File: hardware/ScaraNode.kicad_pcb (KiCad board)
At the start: 2 copper layers, 75.8 x 64 mm, 40 parts, among them J1 FIM1, J2 FIM2, J3 NTC, J4 DM556, J5 24V, J6 MOTOR, J7 FAN 24V, U1 RP2040-Zero, U2 74ACT245, U4 TMC2209

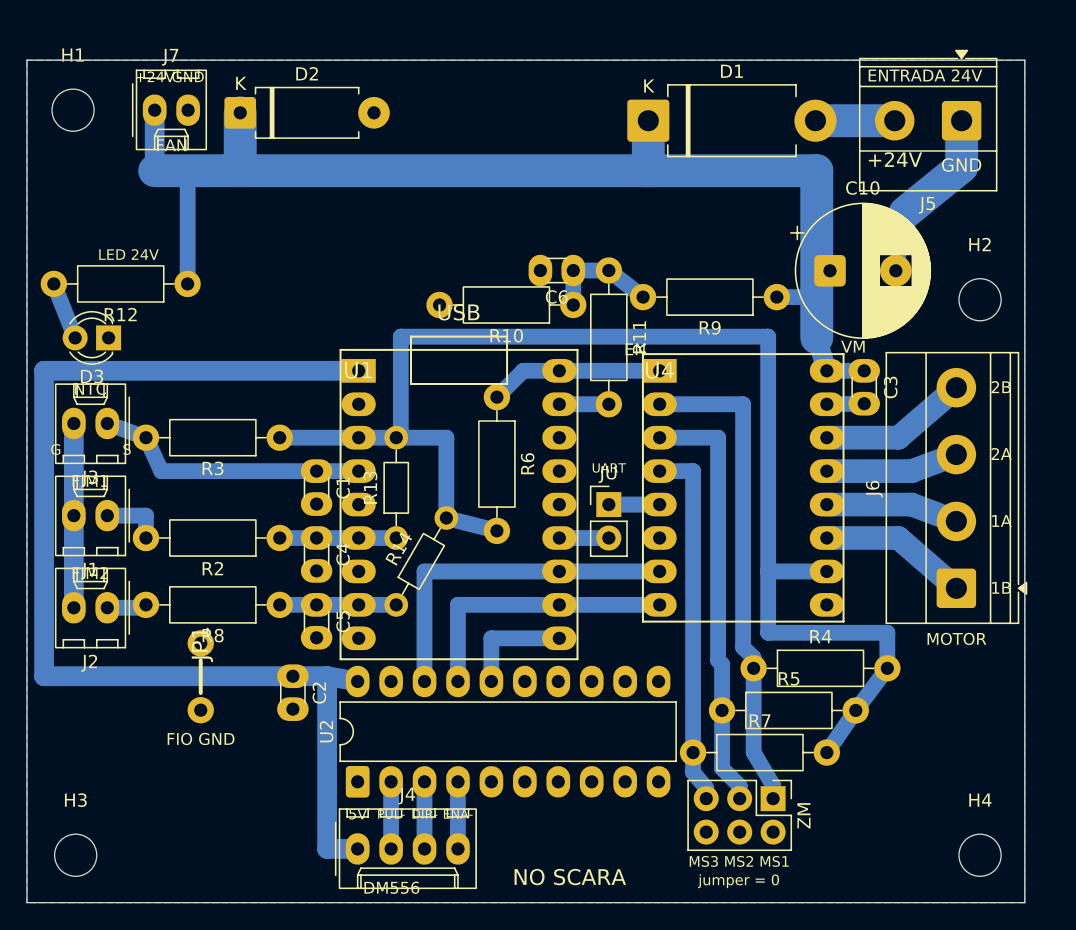
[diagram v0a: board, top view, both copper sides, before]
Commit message: docs(placa): corrige BOM e publica ScaraNode v15
Conectores JST XH (peça real), 74ACT245 soldado direto sem soquete,
borne 24 V verde e motor azul, resistores com faixas de cor por valor,
pinagem desenhada do RP2040-Zero e TMC2209 no lugar de fotos erradas.

Co-Authored-By: Claude Opus 5.5 <noreply@anthropic.com>
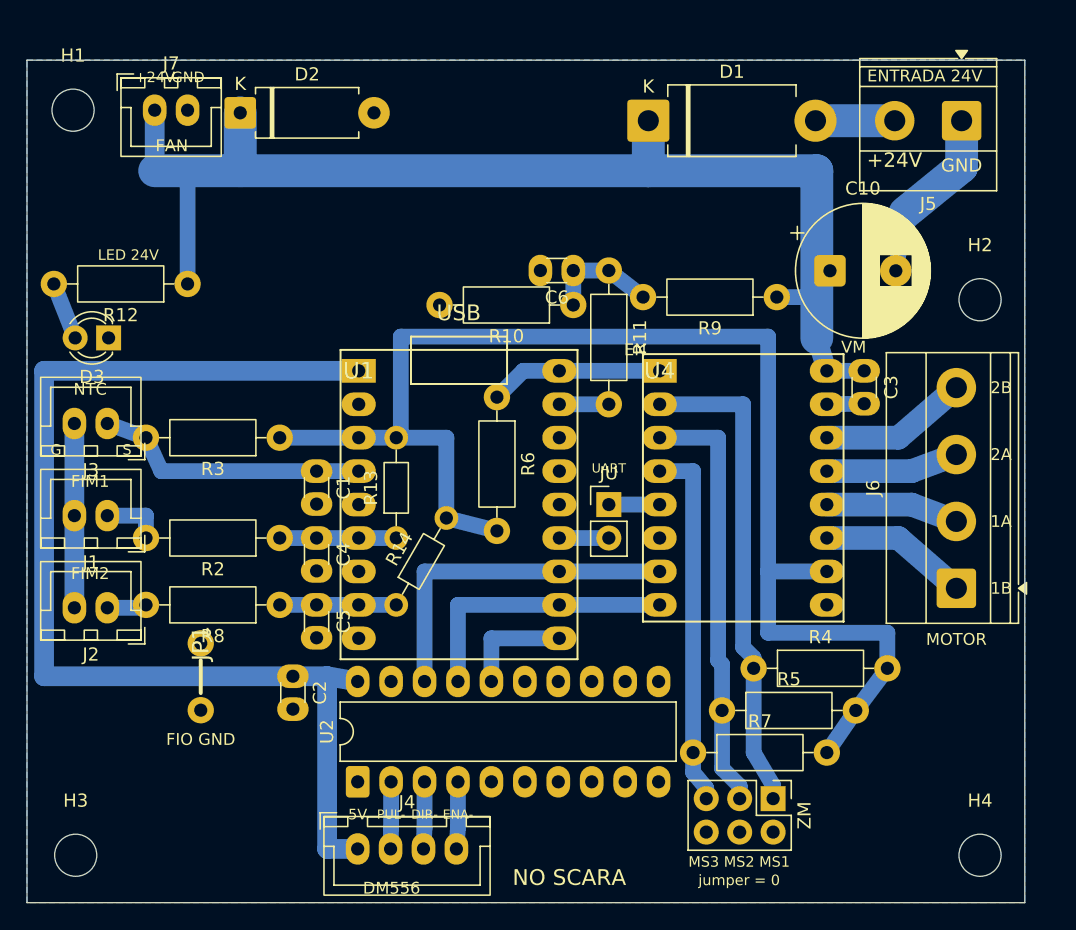
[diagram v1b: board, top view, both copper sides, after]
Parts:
- J1, J2, J3, J7: footprint Molex_KK-254_AE-6410-02A_1x02_P2.54mm_Vertical -> JST_XH_B2B-XH-A_1x02_P2.50mm_Vertical
- J4: footprint Molex_KK-254_AE-6410-04A_1x04_P2.54mm_Vertical -> JST_XH_B4B-XH-A_1x04_P2.50mm_Vertical

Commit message: docs(placa): publica ScaraNode v16
Placa 76 x 64 mm com furos M3 em retângulo de 69 x 57 mm e DXF mecânico,
74ACT245 em soquete DIP-20, borne do motor KF128 azul, NTC separado dos
fins de curso e LED de 5 mm.

Co-Authored-By: Claude Opus 5.5 <noreply@anthropic.com>
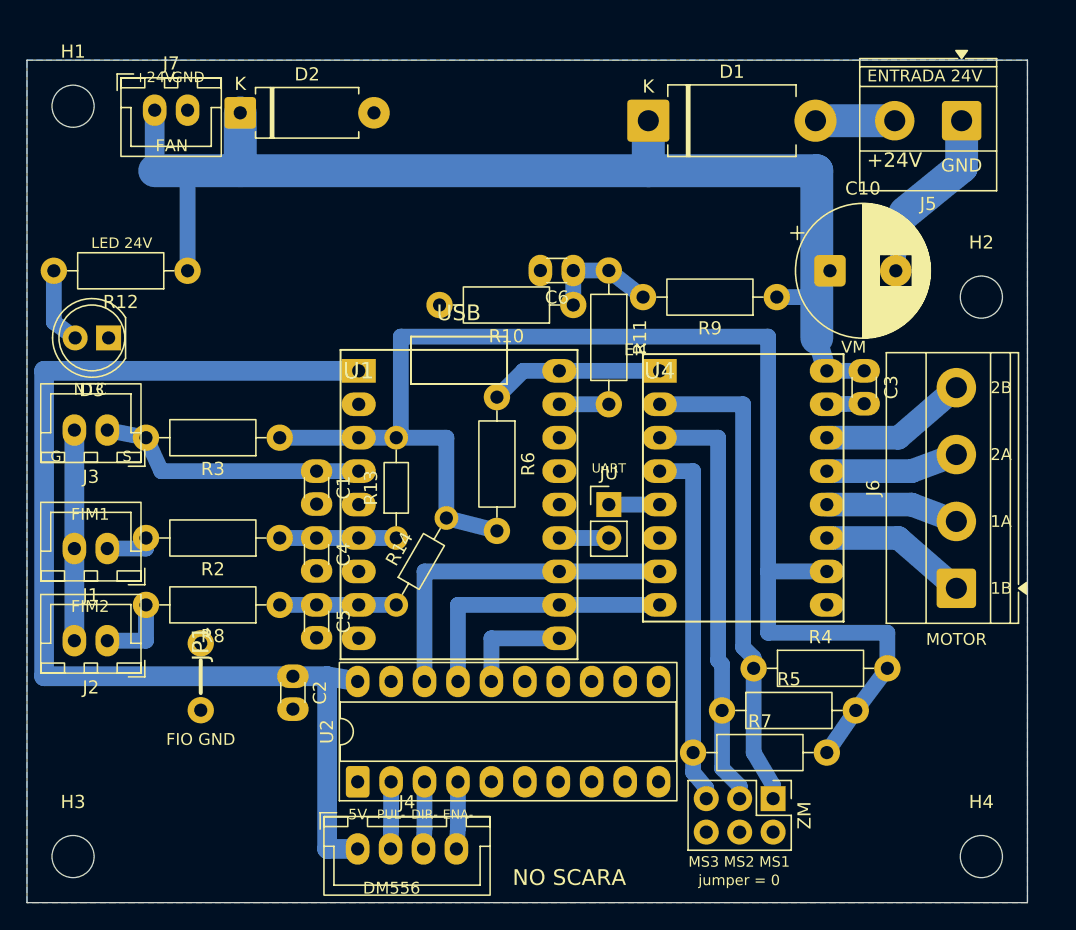
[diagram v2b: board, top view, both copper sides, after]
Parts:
- D3: footprint LED_D3.0mm -> LED_D5.0mm
- U2: footprint DIP-20_W7.62mm_LongPads -> DIP-20_W7.62mm_Socket_LongPads
- moved J1 2.50 mm to (40.9, 91.5)
- moved J2 2.50 mm to (40.9, 98.5)
- moved R12 1.00 mm to (47.0, 70.4)
- moved J3 0.50 mm to (40.9, 82.5)
- moved H1 0.30 mm to (38.3, 57.9)
- moved H3 0.22 mm to (38.3, 114.9)
- moved H2 0.22 mm to (107.3, 72.4)
- moved H4 0.14 mm to (107.3, 114.9)
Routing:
- net SW2_IN: track 3.16 -> 5.66 mm
- net GND: track 30.3 -> 32.3 mm
- net LED_A: track 4.41 -> 5.92 mm
- net 24V: track 93.9 -> 92.9 mm
- net SW1_IN: track 4.64 -> 3.74 mm
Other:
- board size 75.8 x 64 mm -> 76 x 64 mm

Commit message: docs(placa): publica ScaraNode v17 com esquemático
Co-Authored-By: Claude Opus 5.5 <noreply@anthropic.com>
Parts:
- removed JP1: JUMPER GND, ScaraNode:WireLink_P5.08mm
- removed the JU at (79.0, 88.2)
- removed the ZM at (91.5, 110.5)
- added JU: UART, Connector_PinHeader_2.54mm:PinHeader_1x02_P2.54mm_Vertical, F.Cu at (79.0, 88.2)
- added ZM: MICROPASSO, Connector_PinHeader_2.54mm:PinHeader_2x03_P2.54mm_Vertical, F.Cu at (91.5, 110.5)
- C1, C2, C3, C4, C5, C6: footprint C_Disc_D3.0mm_W1.6mm_P2.50mm -> Capacitor_THT:C_Disc_D3.0mm_W1.6mm_P2.50mm
- C10: footprint CP_Radial_D10.0mm_P5.00mm -> Capacitor_THT:CP_Radial_D10.0mm_P5.00mm
- D1: footprint D_DO-201AD_P12.70mm_Horizontal -> Diode_THT:D_DO-201AD_P12.70mm_Horizontal
- D2: footprint D_DO-15_P10.16mm_Horizontal -> Diode_THT:D_DO-15_P10.16mm_Horizontal
- D3: footprint LED_D5.0mm -> LED_THT:LED_D5.0mm
- H1, H2, H3, H4: footprint MountingHole_3.2mm_M3 -> MountingHole:MountingHole_3.2mm_M3
- J1, J2, J3, J7: footprint JST_XH_B2B-XH-A_1x02_P2.50mm_Vertical -> Connector_JST:JST_XH_B2B-XH-A_1x02_P2.50mm_Vertical
- J4: footprint JST_XH_B4B-XH-A_1x04_P2.50mm_Vertical -> Connector_JST:JST_XH_B4B-XH-A_1x04_P2.50mm_Vertical
- J5: footprint TerminalBlock_Phoenix_MKDS-1,5-2-5.08_1x02_P5.08mm_Horizontal -> TerminalBlock_Phoenix:TerminalBlock_Phoenix_MKDS-1,5-2-5.08_1x02_P5.08mm_Horizontal
- J6: footprint TerminalBlock_Phoenix_MKDS-1,5-4-5.08_1x04_P5.08mm_Horizontal -> TerminalBlock_Phoenix:TerminalBlock_Phoenix_MKDS-1,5-4-5.08_1x04_P5.08mm_Horizontal
- R10, R11, R12, R2, R3, R4, R5, R6, R7, R8, R9: footprint R_Axial_DIN0207_L6.3mm_D2.5mm_P10.16mm_Horizontal -> Resistor_THT:R_Axial_DIN0207_L6.3mm_D2.5mm_P10.16mm_Horizontal
- R13, R14: footprint R_Axial_DIN0204_L3.6mm_D1.6mm_P7.62mm_Horizontal -> Resistor_THT:R_Axial_DIN0207_L6.3mm_D2.5mm_P10.16mm_Horizontal
- U2: footprint DIP-20_W7.62mm_Socket_LongPads -> Package_DIP:DIP-20_W7.62mm_Socket_LongPads
- moved R6 1.30 mm to (71.8, 80.0)
- moved C2 1.00 mm to (55.0, 102.2)
- moved U2 1.00 mm to (59.9, 110.2)
- moved R2 0.80 mm to (54.8, 90.7)
- moved R3 0.80 mm to (54.8, 83.1)
- moved R8 0.80 mm to (54.8, 95.8)
- moved C1 0.10 mm to (56.9, 85.6)
- moved C4 0.10 mm to (56.9, 90.7)
- moved C5 0.10 mm to (56.9, 95.8)
- turned R13 to 50 degrees
- turned R14 to 50 degrees
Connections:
- U1 pad GP14: (no net) -> unconnected-(U1-PadGP14)
- U1 pad GP2: (no net) -> unconnected-(U1-PadGP2)
- U1 pad GP26: (no net) -> unconnected-(U1-PadGP26)
- U1 pad GP28: (no net) -> unconnected-(U1-PadGP28)
- U1 pad GP3: (no net) -> unconnected-(U1-PadGP3)
- U1 pad GP4: (no net) -> unconnected-(U1-PadGP4)
- U2 pad 5: (no net) -> unconnected-(U2-A4-Pad5)
- U2 pad 6: (no net) -> unconnected-(U2-A5-Pad6)
- U2 pad 7: (no net) -> unconnected-(U2-A6-Pad7)
- U2 pad 8: (no net) -> unconnected-(U2-A7-Pad8)
- U2 pad 9: (no net) -> unconnected-(U2-A8-Pad9)
- U4 pad 6: (no net) -> unconnected-(U4-SLP/CLK-Pad6)
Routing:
- net 3V3: track 104.9 -> 98.7 mm
- net STP: track 26.2 -> 27.2 mm
- net PUL: track 5.10 -> 4.10 mm
- net ENAO: track 5.10 -> 4.10 mm
- net ENA: track 8.44 -> 9.44 mm
- net DIRO: track 5.10 -> 4.10 mm
- net DIR: track 21.1 -> 22.1 mm
- net SW2: track 8.85 -> 8.05 mm
- net SW1: track 8.85 -> 8.05 mm
- net SW2_IN: track 5.66 -> 6.46 mm
- net SW1_IN: track 3.74 -> 4.54 mm
- net NTC: track 20.8 -> 21.4 mm
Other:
- board text removed: "FIO GND"

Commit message: docs(placa): publica ScaraNode v18
- Canais independentes: TMC2209 em GP4/GP5/GP0 e DM556 em GP6/GP7/GP8;
  uma placa pode mover dois motores ao mesmo tempo.
- UART do TMC2209 no pino 4 do soquete (GP2 via JU); ate a v17 ia ao pino 5.
- Sem o jumper ZM (MS1/MS2 fixos, endereco UART 3).
- Segundo NTC (J8, GP26) e segunda saida de ventoinha (J9).
- Nenhuma curva de trilha de 90 graus.
- Fusivel de 2 A por placa (e 5 A por DM556) numa caixa de fusiveis de
  lamina, documentado no capitulo 6; avisos para nao queimar o driver no
  cfg e no capitulo 7.
- Validada: 128 pinos, ERC e paridade 0, DRC de cobre sem erro.

Co-Authored-By: Claude Opus 5.5 <noreply@anthropic.com>
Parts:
- removed ZM: MICROPASSO, Connector_PinHeader_2.54mm:PinHeader_2x03_P2.54mm_Vertical
- added C7: 100nF, Capacitor_THT:C_Disc_D3.0mm_W1.6mm_P2.50mm, F.Cu at (52.0, 99.6)
- added J8: NTC2, Connector_JST:JST_XH_B2B-XH-A_1x02_P2.50mm_Vertical, F.Cu at (40.9, 94.6)
- added J9: FAN2 24V, Connector_JST:JST_XH_B2B-XH-A_1x02_P2.50mm_Vertical, F.Cu at (65.2, 58.2)
- added R15: 100k, Resistor_THT:R_Axial_DIN0207_L6.3mm_D2.5mm_P10.16mm_Horizontal, F.Cu at (56.9, 83.1)
- J3: value NTC -> NTC1
- moved C1 8.90 mm to (48.0, 85.6)
- moved C4 4.16 mm to (53.5, 88.3), turned to 180 degrees
- moved J1 2.95 mm to (40.9, 88.5)
- moved JU 2.54 mm to (79.0, 85.6), turned to 180 degrees
- moved J2 2.15 mm to (40.9, 100.7)
- moved C2 1.10 mm to (55.0, 103.3)
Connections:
- R7 pad 1: MS3 -> UART_TMC
- U1 pad GP2: unconnected-(U1-PadGP2) -> UART
- U1 pad GP26: unconnected-(U1-PadGP26) -> NTC2
- U1 pad GP4: unconnected-(U1-PadGP4) -> STP
- U1 pad GP5: UART -> DIR
- U1 pad GP6: STP -> DM_STP
- U1 pad GP7: DIR -> DM_DIR
- U2 pad 17: DIR -> DM_DIR
- U2 pad 18: STP -> DM_STP
- U4 pad 4: MS3 -> UART_TMC
- U4 pad 5: UART_TMC -> unconnected-(U4-RST/PDN-Pad5)
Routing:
- net MS3: track 27.8 -> 0.00 mm
- net NTC2: track 0.00 -> 25.7 mm
- net UART_TMC: track 3.86 -> 27.2 mm
- net DM_STP: track 0.00 -> 19.0 mm
- net STP: track 27.2 -> 11.5 mm
- net DM_DIR: track 0.00 -> 13.9 mm
- net MS1: track 37.0 -> 26.1 mm
- net DIR: track 22.1 -> 11.5 mm
- net MS2: track 32.5 -> 24.7 mm
- net 24V: track 92.9 -> 96.3 mm
- net SW1: track 8.05 -> 10.8 mm
- net 3V3: track 98.7 -> 96.4 mm
- net GND: track 32.3 -> 34.5 mm
- net 5V: track 86.4 -> 84.8 mm
- net SW2_IN: track 6.46 -> 8.03 mm
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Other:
- board text added: "NTC1"
- board text added: "NTC2"
- board text removed: "MS3 MS2 MS1"
- board text removed: "NTC"
- board text removed: "jumper = 0"

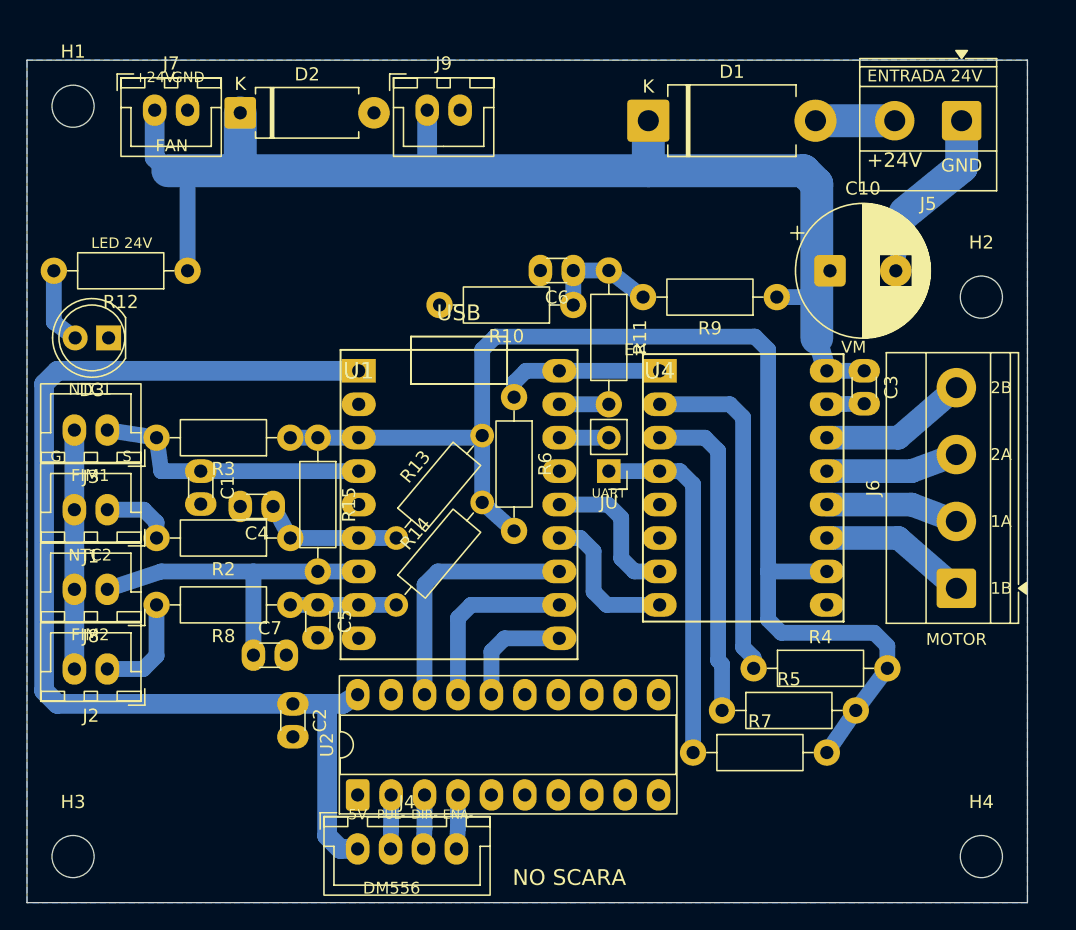
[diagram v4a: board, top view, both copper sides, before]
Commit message: docs(placa): conectores plugaveis 2EDG e furos M3 esquadrados (v18)
- J5 24 V: 2EDGRC 90 graus + plugue 2EDGK, entrando pela borda de cima.
- J6 motor: 2EDGVC vertical + plugue 2EDGK, fio saindo para a direita.
- Os quatro furos M3 nos cantos (retangulo de 69 x 57 mm); DXF atualizado.
- C10 a 1,4 mm do J5. Validada: 128 pinos, DRC de cobre sem erro.

Co-Authored-By: Claude Opus 5.5 <noreply@anthropic.com>
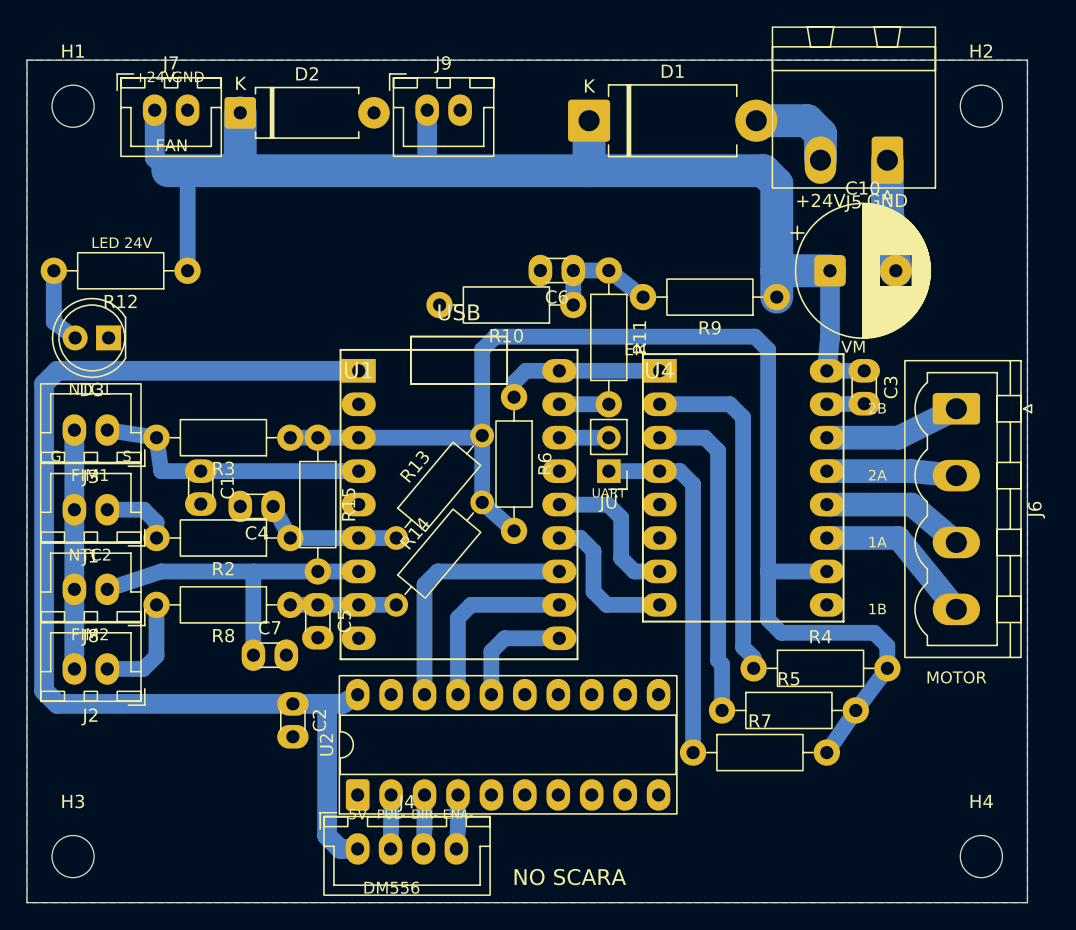
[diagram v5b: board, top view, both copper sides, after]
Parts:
- J5: footprint TerminalBlock_Phoenix:TerminalBlock_Phoenix_MKDS-1,5-2-5.08_1x02_P5.08mm_Horizontal -> Connector_Phoenix_MSTB:PhoenixContact_MSTBA_2,5_2-G-5,08_1x02_P5.08mm_Horizontal
- J6: footprint TerminalBlock_Phoenix:TerminalBlock_Phoenix_MKDS-1,5-4-5.08_1x04_P5.08mm_Horizontal -> Connector_Phoenix_MSTB:PhoenixContact_MSTBVA_2,5_4-G-5,08_1x04_P5.08mm_Vertical
- moved H2 14.5 mm to (107.3, 57.9)
- moved J6 13.6 mm to (105.4, 80.9), turned to -90 degrees
- moved J5 6.39 mm to (100.2, 62.0)
- moved D1 4.50 mm to (77.5, 59.0)
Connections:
- J6 pad 1: M1B -> M2B
- J6 pad 2: M1A -> M2A
- J6 pad 3: M2A -> M1A
- J6 pad 4: M2B -> M1B
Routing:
- net GND: track 34.5 -> 29.4 mm
- net 24V_IN: track 6.02 -> 7.29 mm
- net M1B: track 11.3 -> 12.4 mm
- net 24V: track 96.3 -> 95.2 mm
- net M2B: track 11.3 -> 10.4 mm
- net M1A: track 10.1 -> 10.9 mm
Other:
- board text removed: "ENTRADA 24V"
